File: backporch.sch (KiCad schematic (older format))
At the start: 31 parts, among them J1 MD-90SM, J2 MD-80SM, J3 DB15_Female_HighDensity_Mount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, J4 35RAPC4BH3, U1 EL1883ISZ

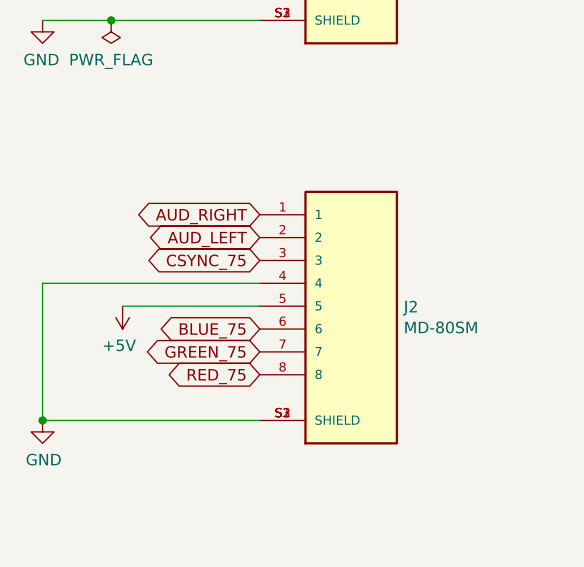
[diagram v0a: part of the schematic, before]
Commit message: Backporch 0.2: Swap pin 3 and 5 on mini-DIN 8
For some reason, CUI devices labeling of their pins for their mini-DIN 8
is different from everybody else's and also different from their other
mini DIN connectors.

This fixes a major issue where +5V and sync were swapped on the
mini-DIN 8 connector.
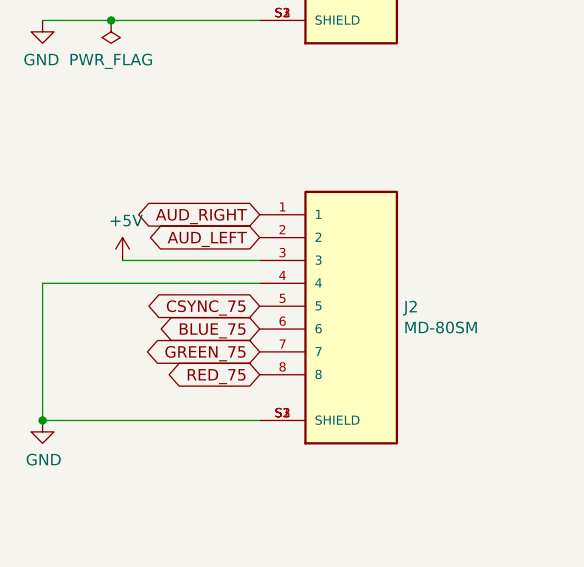
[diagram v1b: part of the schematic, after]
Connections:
- net +5V: now also J2.3; no longer J2.5
- net CSYNC_75: now also J2.5; no longer J2.3
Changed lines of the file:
@@
 Sheet 1 1
 Title "Backporch retroconsole output to RGBS + Scart"
-Date "2021-02-05"
-Rev "0"
+Date "2021-02-23"
+Rev "0.2"
 Comp ""
 Comment1 "https://github.com/semi-simple/backporch"
@@
 Text GLabel 1650 3300 0    50   BiDi ~ 0
 AUD_LEFT
-Text GLabel 1650 3400 0    50   BiDi ~ 0
+Text GLabel 1650 3600 0    50   BiDi ~ 0
 CSYNC_75
 Wire Wire Line
-	1650 3600 1050 3600
+	1650 3400 1050 3400
 $Comp
 L power:+5V #PWR03
 U 1 1 60148F1A
-P 1050 3600
-F 0 "#PWR03" H 1050 3450 50  0001 C CNN
-F 1 "+5V" H 1065 3773 50  0000 C CNN
-F 2 "" H 1050 3600 50  0001 C CNN
-F 3 "" H 1050 3600 50  0001 C CNN
-	1    1050 3600
-	-1   0    0    1
+P 1050 3400
+F 0 "#PWR03" H 1050 3250 50  0001 C CNN
+F 1 "+5V" H 1065 3573 50  0000 C CNN
+F 2 "" H 1050 3400 50  0001 C CNN
+F 3 "" H 1050 3400 50  0001 C CNN
+	1    1050 3400
+	1    0    0    -1
 $EndComp
 Text GLabel 1650 3700 0    50   BiDi ~ 0

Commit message: Update DE-15/VGA connector footprint
KiCad's DE-15 footprint is not correct for right angle connectors,
making it difficult to fit standard connectors.

Use VGA_CONN footprint from the OSSC project at
https://github.com/marqs85/ossc_pcb instead as a workaround.
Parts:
- J3: footprint Connector_Dsub:DSUB-15-HD_Female_Horizontal_P2.29x1.98mm_EdgePinOffset8.35mm_Housed_MountingHolesOffset10.89mm -> VGA-from-OSSC:VGA_CONN
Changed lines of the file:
@@
 F 0 "J3" H 8200 3317 50  0000 C CNN
 F 1 "DB15_Female_HighDensity_MountingHoles" H 8200 3226 50  0000 C CNN
-F 2 "Connector_Dsub:DSUB-15-HD_Female_Horizontal_P2.29x1.98mm_EdgePinOffset8.35mm_Housed_MountingHolesOffset10.89mm" H 7250 2850 50  0001 C CNN
+F 2 "VGA-from-OSSC:VGA_CONN" H 7250 2850 50  0001 C CNN
 F 3 " ~" H 7250 2850 50  0001 C CNN
 F 4 "AE11024-ND" H 8200 2450 50  0001 C CNN "Digi-key part number"

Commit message: Footprints: add external footprints to project
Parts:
- J1: footprint MD90:CUI_MD-90SM -> project-footprints:CUI_MD-90SM
- J2: footprint MD80:CUI_MD-80SM -> project-footprints:CUI_MD-80SM
- J3: footprint VGA-from-OSSC:VGA_CONN -> project-footprints:VGA_CONN
- J4: footprint 35RAPC4BH3:SWITCHCRAFT_35RAPC4BH3 -> project-footprints:SWITCHCRAFT_35RAPC4BH3
- U1: footprint EL1883ISZ:SOIC127P600X175-8N -> project-footprints:SOIC127P600X175-8N
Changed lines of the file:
@@
 F 0 "J1" H 1945 2617 50  0000 C CNN
 F 1 "MD-90SM" H 1945 2526 50  0000 C CNN
-F 2 "MD90:CUI_MD-90SM" H 2050 1850 50  0001 L BNN
+F 2 "project-footprints:CUI_MD-90SM" H 2050 1850 50  0001 L BNN
 F 3 "" H 2050 1850 50  0001 L BNN
 F 4 "CP-2290-ND" H 2050 1850 50  0001 C CNN "Digi-key part number"
@@
 F 0 "J3" H 8200 3317 50  0000 C CNN
 F 1 "DB15_Female_HighDensity_MountingHoles" H 8200 3226 50  0000 C CNN
-F 2 "VGA-from-OSSC:VGA_CONN" H 7250 2850 50  0001 C CNN
+F 2 "project-footprints:VGA_CONN" H 7250 2850 50  0001 C CNN
 F 3 " ~" H 7250 2850 50  0001 C CNN
 F 4 "AE11024-ND" H 8200 2450 50  0001 C CNN "Digi-key part number"
@@
 F 0 "U1" H 5050 5720 50  0000 C CNN
 F 1 "EL1883ISZ" H 5050 5629 50  0001 C CNN
-F 2 "EL1883ISZ:SOIC127P600X175-8N" H 5050 5250 50  0001 L BNN
+F 2 "project-footprints:SOIC127P600X175-8N" H 5050 5250 50  0001 L BNN
 F 3 "" H 5050 5250 50  0001 L BNN
 F 4 "EL1883ISZ-ND" H 5050 5250 50  0001 C CNN "Digi-key part number"
@@
 F 0 "J2" H 2280 3596 50  0000 L CNN
 F 1 "MD-80SM" H 2280 3505 50  0000 L CNN
-F 2 "MD80:CUI_MD-80SM" H 2050 3600 50  0001 L BNN
+F 2 "project-footprints:CUI_MD-80SM" H 2050 3600 50  0001 L BNN
 F 3 "" H 2050 3600 50  0001 L BNN
 F 4 "CP-2280-ND" H 2050 3600 50  0001 C CNN "Digi-key part number"
@@
 F 0 "J4" H 7793 4428 50  0000 C CNN
 F 1 "35RAPC4BH3" H 7793 4337 50  0000 C CNN
-F 2 "35RAPC4BH3:SWITCHCRAFT_35RAPC4BH3" H 7750 4050 50  0001 L BNN
+F 2 "project-footprints:SWITCHCRAFT_35RAPC4BH3" H 7750 4050 50  0001 L BNN
 F 3 "" H 7750 4050 50  0001 L BNN
 F 4 "SC1464-ND" H 7750 4050 50  0001 C CNN "Digi-key part number"
